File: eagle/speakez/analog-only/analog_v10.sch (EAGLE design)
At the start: 18 parts, among them U1 ADMP621ACEZ-RL7

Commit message: tiny wiring tweak
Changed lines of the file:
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@@
 </classes>
 <parts>
-<part name="U1" library="InvenSense-INMP621ACEZ-R7" deviceset="ADMP621ACEZ-RL7" device=""/>
+<part name="U1" library="InvenSense-INMP621ACEZ-R7" deviceset="ADMP621ACEZ-RL7" device="" value=""/>
 <part name="SUPPLY1" library="supply2" deviceset="GND" device=""/>
 <part name="SUPPLY2" library="SparkFun-Aesthetics" deviceset="VCC" device=""/>

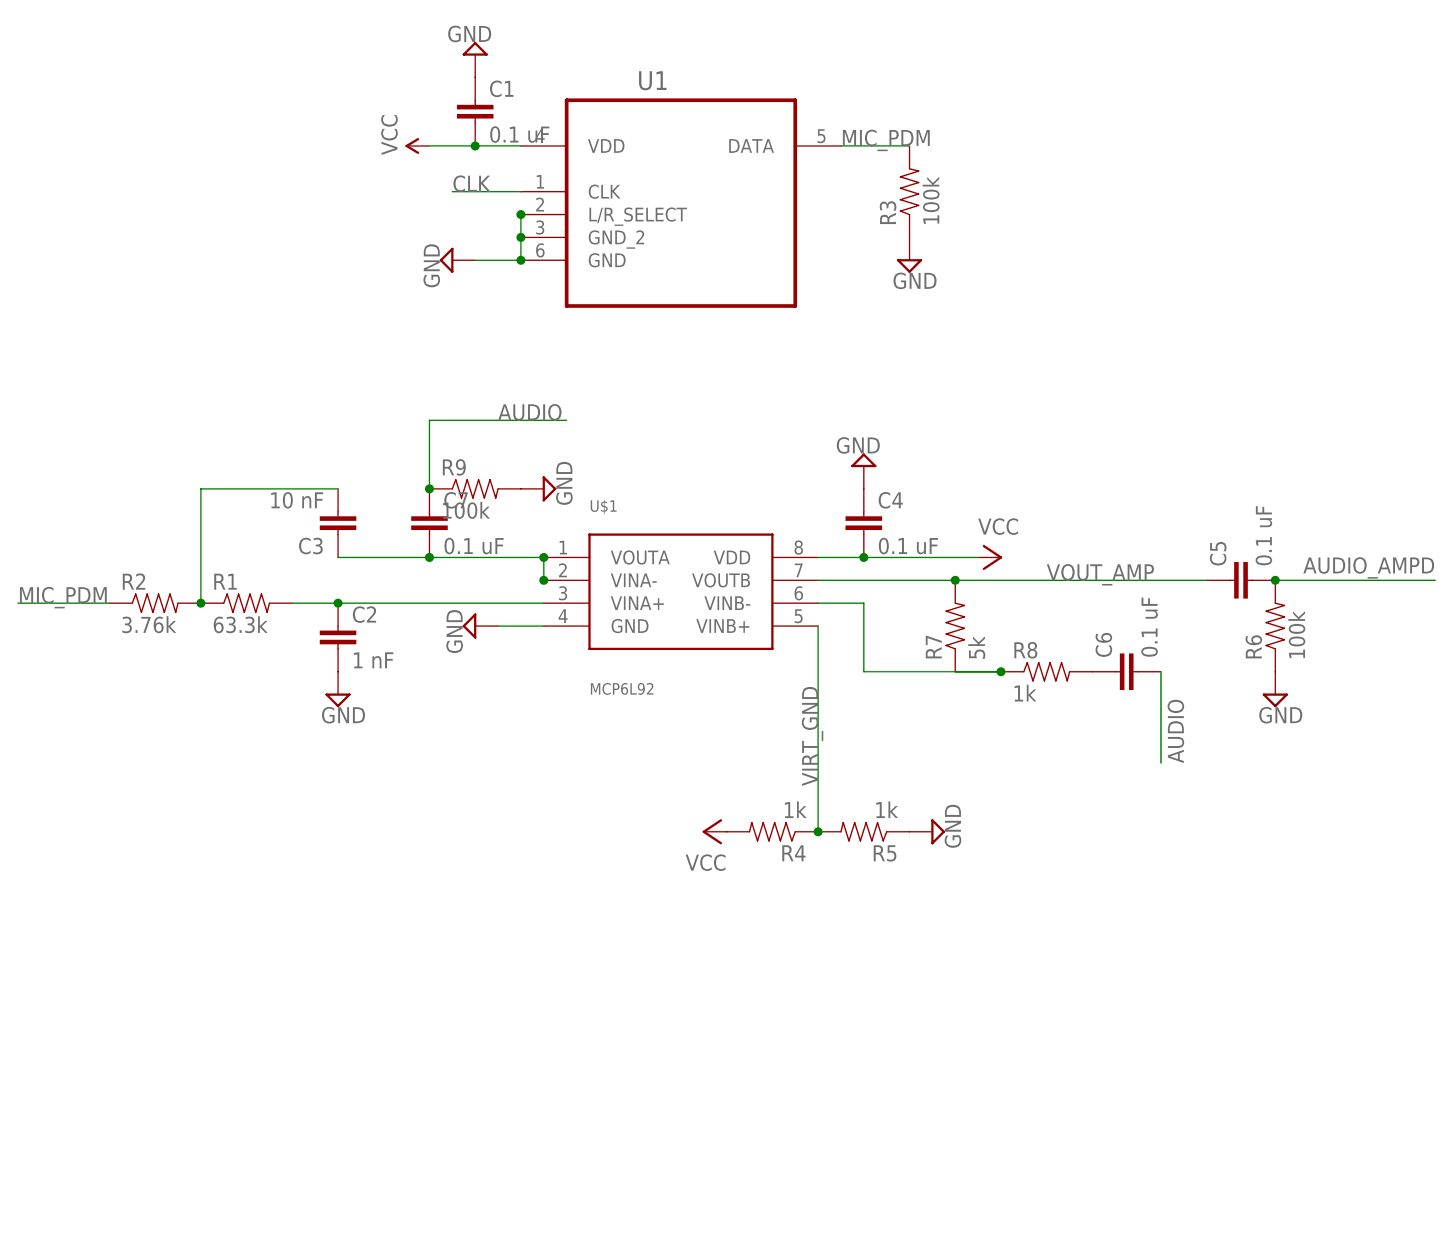
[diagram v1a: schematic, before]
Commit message: Analog Rev 1
also added a ton of library parts
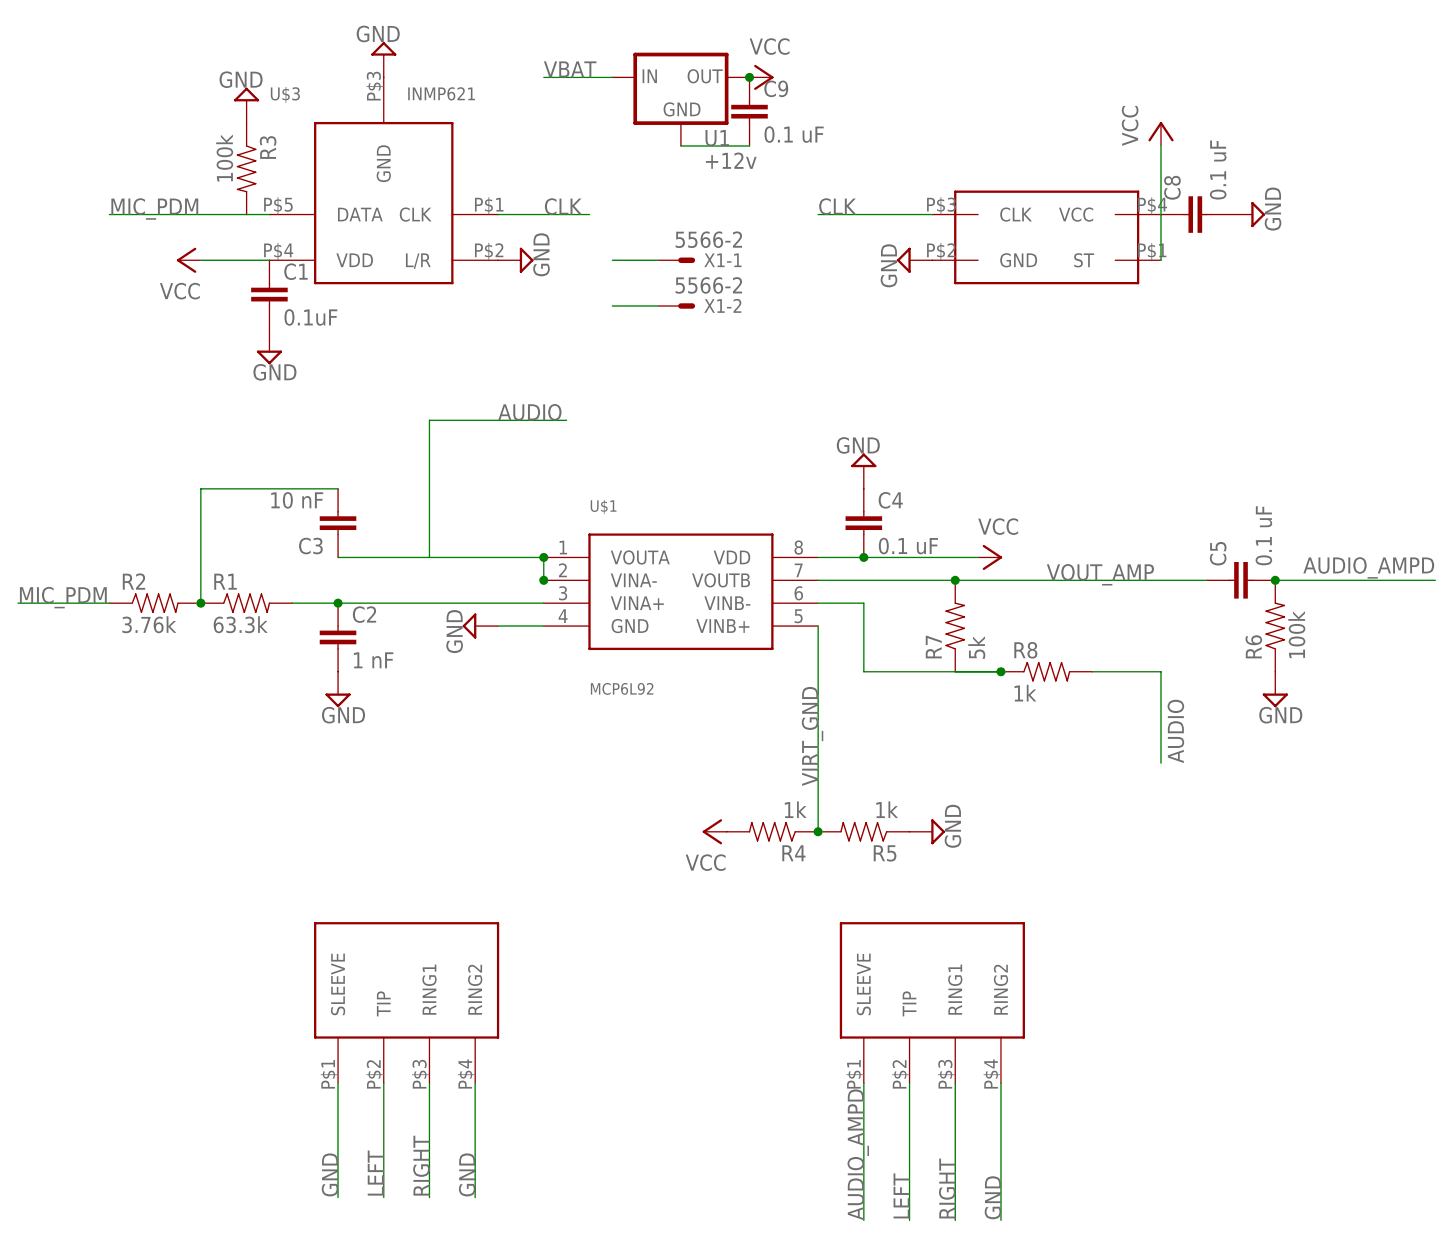
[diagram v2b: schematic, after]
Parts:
- removed C6, C7: 0.1 uF, SparkFun-Passives:CAP0805
- removed R9: 100k, SparkFun-Resistors:RESISTOR0805-RES
- added C8, C9: 0.1 uF, SparkFun-Passives:CAP0805
- added HEADPHONE, RADIO: SJ-43514-SMT, 35mm_audio:SJ-43514-SMT
- added U$2: SG-210STF, crystal-epson:SG-210STF
- added U$3: INMP621, InvenSense-INMP621ACEZ-R7:INMP621
- added X1: 5566-2, con-molex:5566-2
- C1: value 0.1 uF -> 0.1uF
- U1: value ADMP621ACEZ-RL7 -> +12v; device InvenSense-INMP621ACEZ-R7:ADMP621ACEZ-RL7 -> LP38691:V_REG_78XX7812
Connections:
- removed net N$8: C6.1, R8.2
- removed net VOUT_FILTER: C3.1, C7.2, U$1.VINA-, U$1.VOUTA
- new net LEFT: HEADPHONE.TIP, RADIO.TIP
- new net RIGHT: HEADPHONE.RING1, RADIO.RING1
- new net VBAT: U1.IN, X1-1.S
- net AUDIO: now also C3.1, R8.2, U$1.VINA-, U$1.VOUTA; no longer C6.2, C7.1, R9.1
- net AUDIO_AMPD: now also RADIO.SLEEVE
- net CLK: now also U$2.CLK, U$3.CLK; no longer U1.CLK
- net GND: now also C1.2, C8.2, C9.2, HEADPHONE.RING2, HEADPHONE.SLEEVE, RADIO.RING2, U$2.GND, U$3.GND, U$3.L/R, X1-2.S; no longer C1.1, R9.2, U1.GND_2, U1.L/R_SELECT
- net MIC_PDM: now also U$3.DATA; no longer U1.DATA
- net VCC: now also C1.1, C8.1, C9.1, U$2.ST, U$2.VCC, U$3.VDD, U1.OUT; no longer C1.2, U1.VDD
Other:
- moved on the sheet: C1, R3

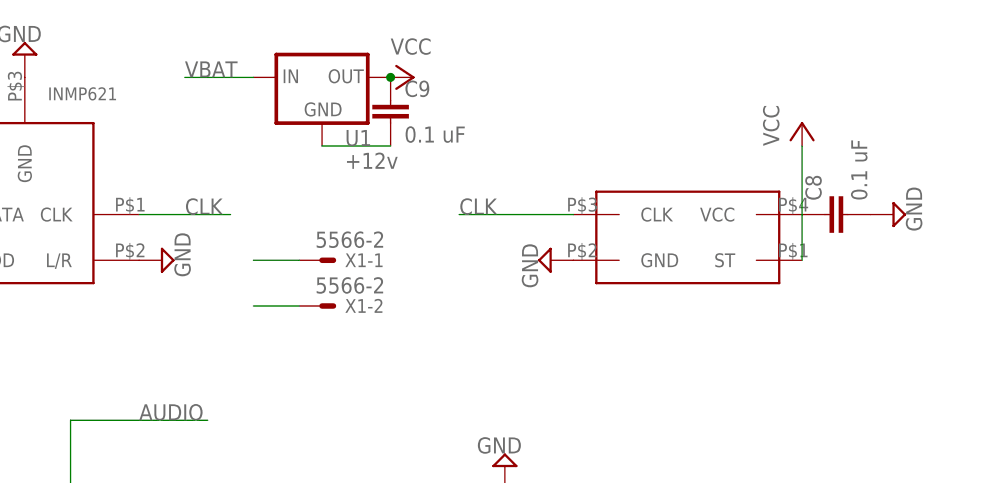
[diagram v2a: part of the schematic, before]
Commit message: Safety diode
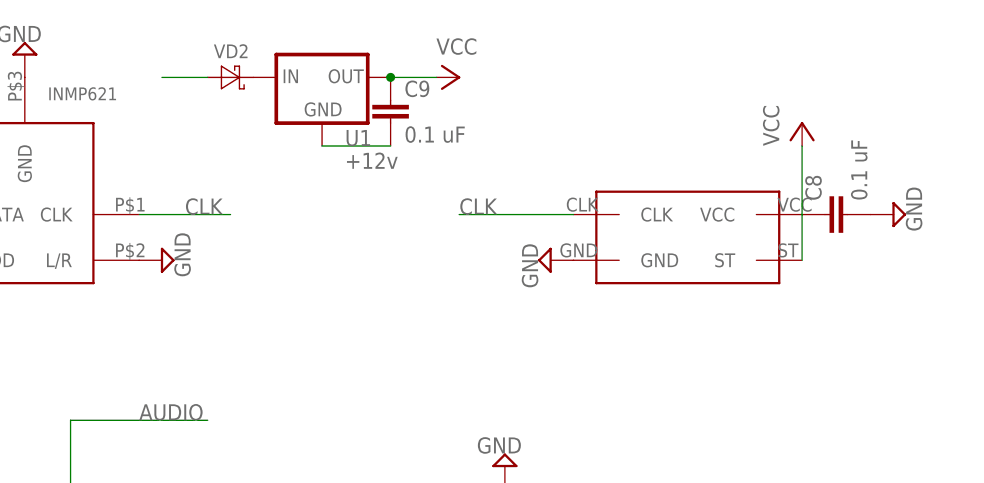
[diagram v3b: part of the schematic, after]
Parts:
- removed X1: 5566-2, con-molex:5566-2
- added VD2: (no value), diode:DIODE-SCHOTTKY-SOD123
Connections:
- new net VBATSAFE: U1.IN, VD2.C
- net GND: no longer X1-2.S
- net VBAT: now also VD2.A; no longer U1.IN, X1-1.S
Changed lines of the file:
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@@
 <?xml version="1.0" encoding="utf-8"?>
 <!DOCTYPE eagle SYSTEM "eagle.dtd">
-<eagle version="7.6.0">
+<eagle version="7.7.0">
 <drawing>
 <settings>
@@
 <part name="HEADPHONE" library="35mm_audio" deviceset="SJ-43514-SMT" device=""/>
 <part name="RADIO" library="35mm_audio" deviceset="SJ-43514-SMT" device=""/>
-<part name="X1" library="con-molex" deviceset="5566-2" device=""/>
+<part name="VD2" library="diode" deviceset="DIODE-SCHOTTKY-" device="SOD123"/>
 </parts>
 <sheets>
@@
 <instance part="U1" gate="G$1" x="63.5" y="119.38"/>
 <instance part="C9" gate="G$1" x="71.12" y="114.3"/>
-<instance part="P+5" gate="VCC" x="73.66" y="119.38" rot="R270"/>
+<instance part="P+5" gate="VCC" x="78.74" y="119.38" rot="R270"/>
 <instance part="HEADPHONE" gate="G$1" x="25.4" y="12.7"/>
 <instance part="RADIO" gate="G$1" x="83.82" y="12.7"/>
-<instance part="X1" gate="-1" x="63.5" y="99.06"/>
-<instance part="X1" gate="-2" x="63.5" y="93.98"/>
+<instance part="VD2" gate="G$1" x="53.34" y="119.38"/>
 </instances>
 <busses>
@@
 <wire x1="99.06" y1="7.62" x2="99.06" y2="-7.62" width="0.1524" layer="91"/>
 <label x="99.06" y="-7.62" size="1.778" layer="95" rot="R90"/>
-</segment>
-<segment>
-<pinref part="X1" gate="-2" pin="S"/>
-<wire x1="60.96" y1="93.98" x2="55.88" y2="93.98" width="0.1524" layer="91"/>
 </segment>
 </net>
@@
 <pinref part="C9" gate="G$1" pin="1"/>
 <pinref part="P+5" gate="VCC" pin="VCC"/>
+<wire x1="76.2" y1="119.38" x2="71.12" y2="119.38" width="0.1524" layer="91"/>
 <junction x="71.12" y="119.38"/>
-<pinref part="P+5" gate="VCC" pin="VCC"/>
 </segment>
 </net>
@@
 </segment>
 </net>
-<net name="VBAT" class="0">
-<segment>
-<pinref part="U1" gate="G$1" pin="IN"/>
-<wire x1="55.88" y1="119.38" x2="48.26" y2="119.38" width="0.1524" layer="91"/>
-<label x="48.26" y="119.38" size="1.778" layer="95"/>
-</segment>
-<segment>
-<pinref part="X1" gate="-1" pin="S"/>
-<wire x1="60.96" y1="99.06" x2="55.88" y2="99.06" width="0.1524" layer="91"/>
-</segment>
-</net>
 <net name="RIGHT" class="0">
 <segment>
@@
 </segment>
 </net>
+<net name="VBATSAFE" class="0">
+<segment>
+<pinref part="U1" gate="G$1" pin="IN"/>
+<pinref part="VD2" gate="G$1" pin="C"/>
+</segment>
+</net>
+<net name="VBAT" class="0">
+<segment>
+<pinref part="VD2" gate="G$1" pin="A"/>
+<wire x1="50.8" y1="119.38" x2="45.72" y2="119.38" width="0.1524" layer="91"/>
+</segment>
+</net>
